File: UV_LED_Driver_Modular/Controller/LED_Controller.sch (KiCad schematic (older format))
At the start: 9 parts, among them J1 Barrel_Jack, J2 Conn_01x05, SW1 SW_SPST, U1 STM32L011D4Px, U2 LP3992-33B5F

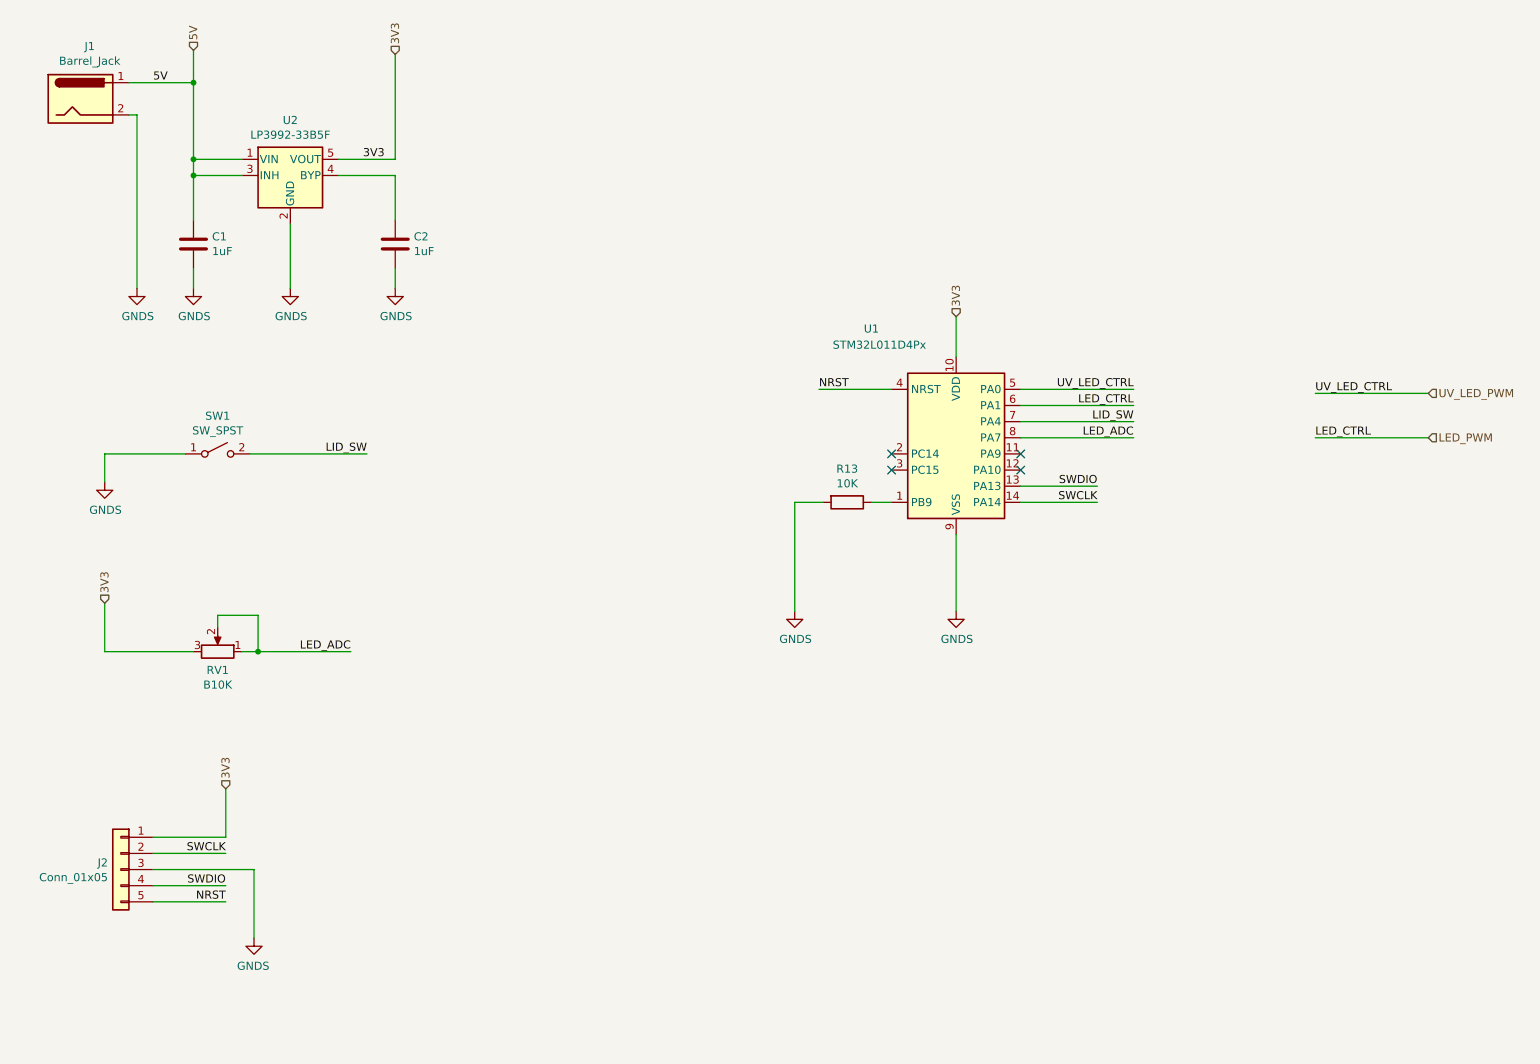
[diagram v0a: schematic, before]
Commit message: Changed TO225 NPN (MJE340) to SOT223 NPN (PZT2222A)
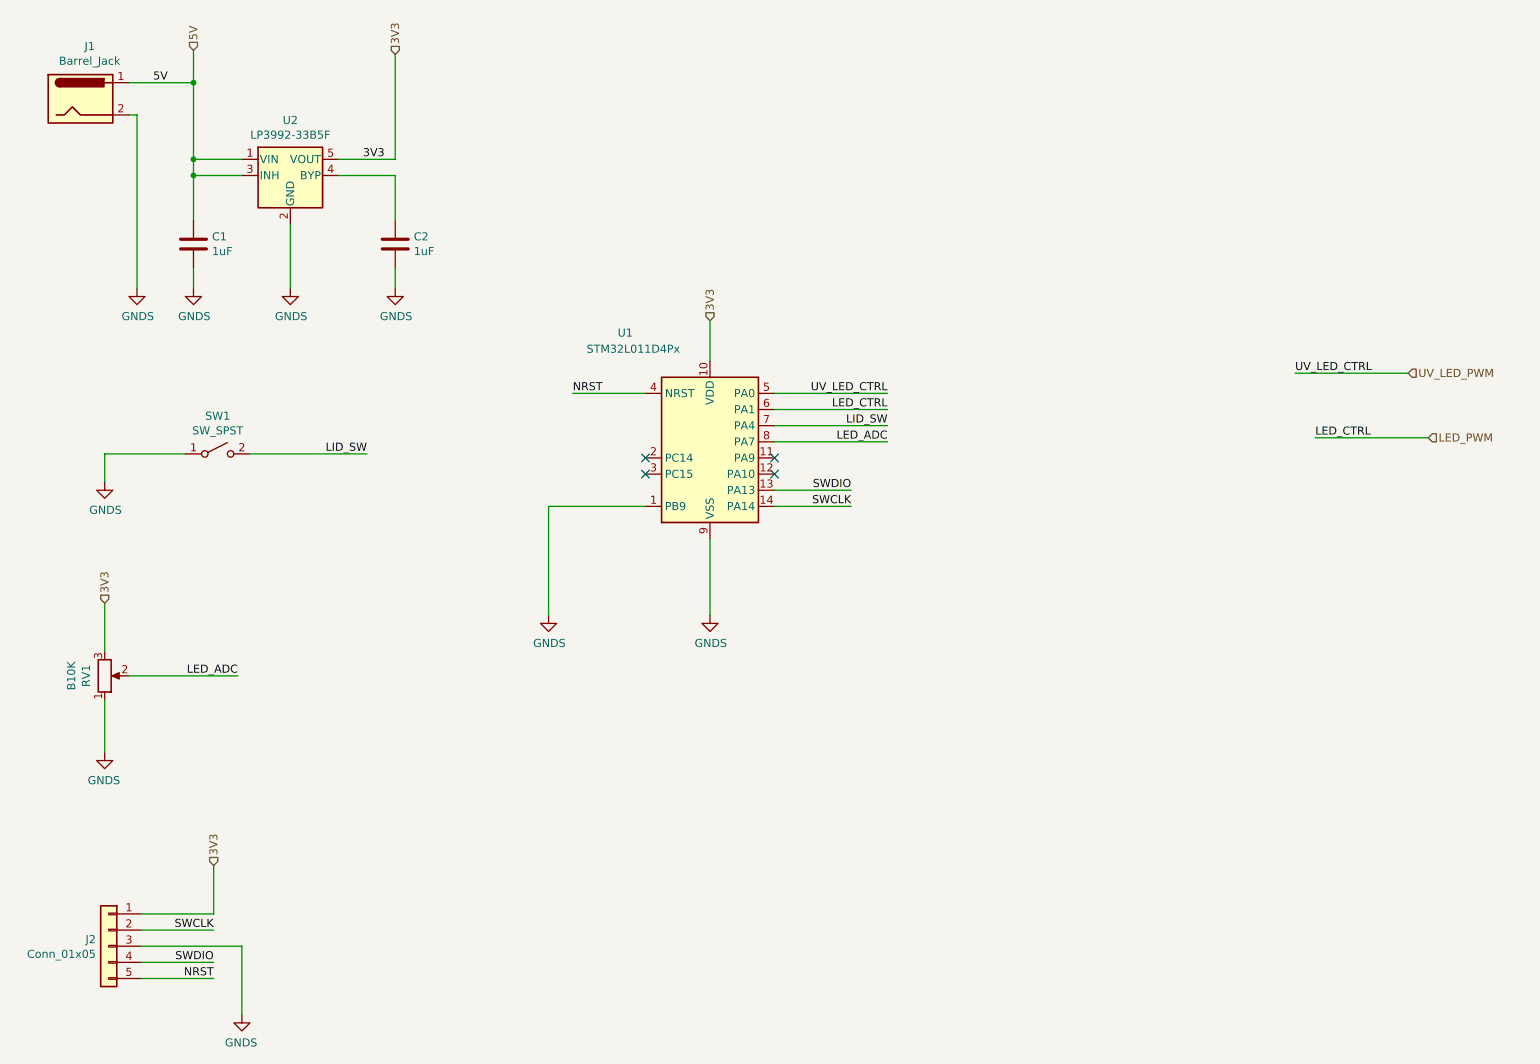
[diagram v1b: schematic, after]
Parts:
- removed R13: 10K, Resistor_SMD:R_1206_3216Metric_Pad1.42x1.75mm_HandSolder, symbol Device:R
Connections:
- net GNDS: now also RV1.1, U1.1 (PB9)
- net LED_ADC: no longer RV1.1
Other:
- moved on the sheet: J2, RV1, U1
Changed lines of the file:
@@
 $Descr A4 11693 8268
 encoding utf-8
-Sheet 6 2
+Sheet 2 2
 Title ""
 Date ""
@@
 $EndDescr
 Wire Wire Line
-	2075 6025 2525 6025
-Wire Wire Line
-	2075 6125 2525 6125
-Text Label 2525 6125 2    50   ~ 0
+	2000 6500 2450 6500
+Wire Wire Line
+	2000 6600 2450 6600
+Text Label 2450 6600 2    50   ~ 0
 SWCLK
-Text Label 2525 6325 2    50   ~ 0
+Text Label 2450 6800 2    50   ~ 0
 SWDIO
-Text Label 2525 6425 2    50   ~ 0
+Text Label 2450 6900 2    50   ~ 0
 NRST
 $Comp
 L Connector_Generic:Conn_01x05 J2
 U 1 1 5EA63B2F
-P 1875 6225
-F 0 "J2" H 1955 6267 50  0000 L CNN
-F 1 "Conn_01x05" H 1955 6176 50  0000 L CNN
-F 2 "Connector_Molex:Molex_KK-254_AE-6410-05A_1x05_P2.54mm_Vertical" H 1875 6225 50  0001 C CNN
-F 3 "~" H 1875 6225 50  0001 C CNN
-	1    1875 6225
+P 1800 6700
+F 0 "J2" H 1880 6742 50  0000 L CNN
+F 1 "Conn_01x05" H 1880 6651 50  0000 L CNN
+F 2 "Connector_Molex:Molex_KK-254_AE-6410-05A_1x05_P2.54mm_Vertical" H 1800 6700 50  0001 C CNN
+F 3 "~" H 1800 6700 50  0001 C CNN
+	1    1800 6700
 	-1   0    0    -1
 $EndComp
 Wire Wire Line
-	2525 6325 2075 6325
-Wire Wire Line
-	2075 6425 2525 6425
-Wire Wire Line
-	2075 6225 2700 6225
-Wire Wire Line
-	2700 6225 2700 6650
+	2450 6800 2000 6800
+Wire Wire Line
+	2000 6900 2450 6900
+Wire Wire Line
+	2000 6700 2625 6700
+Wire Wire Line
+	2625 6700 2625 7125
 $Comp
 L power:GNDS #PWR018
 U 1 1 5EA63B39
-P 2700 6650
-F 0 "#PWR018" H 2700 6400 50  0001 C CNN
-F 1 "GNDS" H 2705 6477 50  0000 C CNN
-F 2 "" H 2700 6650 50  0001 C CNN
-F 3 "" H 2700 6650 50  0001 C CNN
-	1    2700 6650
+P 2625 7125
+F 0 "#PWR018" H 2625 6875 50  0001 C CNN
+F 1 "GNDS" H 2630 6952 50  0000 C CNN
+F 2 "" H 2625 7125 50  0001 C CNN
+F 3 "" H 2625 7125 50  0001 C CNN
+	1    2625 7125
 	-1   0    0    -1
 $EndComp
-Text Label 6200 3250 0    50   ~ 0
+Text Label 4675 3275 0    50   ~ 0
 NRST
 Wire Wire Line
-	6650 3250 6200 3250
-Wire Wire Line
-	6650 3950 6525 3950
-Wire Wire Line
-	6050 3950 6050 4625
+	5125 3275 4675 3275
+Wire Wire Line
+	4525 3975 4525 4650
 $Comp
 L power:GNDS #PWR021
 U 1 1 5EA63B43
-P 6050 4625
-F 0 "#PWR021" H 6050 4375 50  0001 C CNN
-F 1 "GNDS" H 6055 4452 50  0000 C CNN
-F 2 "" H 6050 4625 50  0001 C CNN
-F 3 "" H 6050 4625 50  0001 C CNN
-	1    6050 4625
-	1    0    0    -1
-$EndComp
-NoConn ~ 6650 3750
-NoConn ~ 6650 3650
-NoConn ~ 7450 3750
-NoConn ~ 7450 3650
-Wire Wire Line
-	7450 3850 7925 3850
+P 4525 4650
+F 0 "#PWR021" H 4525 4400 50  0001 C CNN
+F 1 "GNDS" H 4530 4477 50  0000 C CNN
+F 2 "" H 4525 4650 50  0001 C CNN
+F 3 "" H 4525 4650 50  0001 C CNN
+	1    4525 4650
+	1    0    0    -1
+$EndComp
+NoConn ~ 5125 3775
+NoConn ~ 5125 3675
+NoConn ~ 5925 3775
+NoConn ~ 5925 3675
+Wire Wire Line
+	5925 3875 6400 3875
 $Comp
 L MCU_ST_STM32L0:STM32L011D4Px U1
 U 1 1 5EA63B4E
-P 7050 3550
-F 0 "U1" H 6525 4225 50  0000 C CNN
-F 1 "STM32L011D4Px" H 6575 4125 50  0000 C CNN
-F 2 "Package_SO:TSSOP-14_4.4x5mm_P0.65mm" H 6750 3050 50  0001 R CNN
-F 3 "http://www.st.com/st-web-ui/static/active/en/resource/technical/document/datasheet/DM00206508.pdf" H 7050 3550 50  0001 C CNN
-	1    7050 3550
-	1    0    0    -1
-$EndComp
-Wire Wire Line
-	7450 3950 7925 3950
-Text Label 7925 3950 2    50   ~ 0
+P 5525 3575
+F 0 "U1" H 5000 4250 50  0000 C CNN
+F 1 "STM32L011D4Px" H 5050 4150 50  0000 C CNN
+F 2 "Package_SO:TSSOP-14_4.4x5mm_P0.65mm" H 5225 3075 50  0001 R CNN
+F 3 "http://www.st.com/st-web-ui/static/active/en/resource/technical/document/datasheet/DM00206508.pdf" H 5525 3575 50  0001 C CNN
+	1    5525 3575
+	1    0    0    -1
+$EndComp
+Wire Wire Line
+	5925 3975 6400 3975
+Text Label 6400 3975 2    50   ~ 0
 SWCLK
-Text Label 7925 3850 2    50   ~ 0
+Text Label 6400 3875 2    50   ~ 0
 SWDIO
 Wire Wire Line
-	7050 3050 7050 2800
-Wire Wire Line
-	7050 4150 7050 4625
+	5525 3075 5525 2825
+Wire Wire Line
+	5525 4175 5525 4650
 $Comp
 L power:GNDS #PWR022
 U 1 1 5EA63B5F
-P 7050 4625
-F 0 "#PWR022" H 7050 4375 50  0001 C CNN
-F 1 "GNDS" H 7055 4452 50  0000 C CNN
-F 2 "" H 7050 4625 50  0001 C CNN
-F 3 "" H 7050 4625 50  0001 C CNN
-	1    7050 4625
+P 5525 4650
+F 0 "#PWR022" H 5525 4400 50  0001 C CNN
+F 1 "GNDS" H 5530 4477 50  0000 C CNN
+F 2 "" H 5525 4650 50  0001 C CNN
+F 3 "" H 5525 4650 50  0001 C CNN
+	1    5525 4650
 	1    0    0    -1
 $EndComp
@@
 LID_SW
 Wire Wire Line
-	7450 3450 8150 3450
-Text Label 8150 3450 2    50   ~ 0
+	5925 3475 6625 3475
+Text Label 6625 3475 2    50   ~ 0
 LID_SW
 $Comp
@@
 	2325 1350 2325 1150
 Connection ~ 2325 1350
-$Comp
-L Device:R R13
-U 1 1 5EA63BD8
-P 6375 3950
-F 0 "R13" V 6168 3950 50  0000 C CNN
-F 1 "10K" V 6259 3950 50  0000 C CNN
-F 2 "Resistor_SMD:R_1206_3216Metric_Pad1.42x1.75mm_HandSolder" V 6305 3950 50  0001 C CNN
-F 3 "~" H 6375 3950 50  0001 C CNN
-	1    6375 3950
-	0    1    1    0
-$EndComp
-Wire Wire Line
-	6225 3950 6050 3950
-Wire Wire Line
-	7450 3250 8150 3250
-Text Label 8150 3250 2    50   ~ 0
+Wire Wire Line
+	5925 3275 6625 3275
+Text Label 6625 3275 2    50   ~ 0
 UV_LED_CTRL
 Wire Wire Line
-	7450 3350 8150 3350
-Text Label 8150 3350 2    50   ~ 0
+	5925 3375 6625 3375
+Text Label 6625 3375 2    50   ~ 0
 LED_CTRL
 Wire Wire Line
-	7450 3550 8150 3550
-Text Label 8150 3550 2    50   ~ 0
+	5925 3575 6625 3575
+Text Label 6625 3575 2    50   ~ 0
 LED_ADC
 $Comp
 L Device:R_POT RV1
 U 1 1 5EA63BE5
-P 2475 4875
-F 0 "RV1" V 2360 4875 50  0000 C CNN
-F 1 "B10K" V 2269 4875 50  0000 C CNN
-F 2 "Connector_Molex:Molex_KK-254_AE-6410-03A_1x03_P2.54mm_Vertical" H 2475 4875 50  0001 C CNN
-F 3 "~" H 2475 4875 50  0001 C CNN
-	1    2475 4875
-	0    1    -1   0
-$EndComp
-Wire Wire Line
-	2625 4875 2725 4875
-Wire Wire Line
-	2325 4875 1775 4875
+P 1775 5025
+F 0 "RV1" V 1660 5025 50  0000 C CNN
+F 1 "B10K" V 1569 5025 50  0000 C CNN
+F 2 "Connector_Molex:Molex_KK-254_AE-6410-03A_1x03_P2.54mm_Vertical" H 1775 5025 50  0001 C CNN
+F 3 "~" H 1775 5025 50  0001 C CNN
+	1    1775 5025
+	1    0    0    1
+$EndComp
 Wire Wire Line
 	1775 4875 1775 4575
-Wire Wire Line
-	2475 4650 2725 4650
-Wire Wire Line
-	2725 4650 2725 4875
-Wire Wire Line
-	2475 4650 2475 4725
-Connection ~ 2725 4875
-Wire Wire Line
-	2725 4875 3300 4875
-Text Label 3300 4875 2    50   ~ 0
+Text Label 2600 5025 2    50   ~ 0
 LED_ADC
-Text HLabel 9975 3275 2    50   Input ~ 0
+Text HLabel 9850 3150 2    50   Input ~ 0
 UV_LED_PWM
 Text HLabel 9975 3550 2    50   Input ~ 0
 LED_PWM
 Wire Wire Line
-	9975 3275 9275 3275
-Text Label 9275 3275 0    50   ~ 0
+	9850 3150 9150 3150
+Text Label 9150 3150 0    50   ~ 0
 UV_LED_CTRL
 Wire Wire Line
@@
 Text Label 3375 1825 0    50   ~ 0
 3V3
-Text HLabel 7050 2800 1    50   Input ~ 0
+Text HLabel 5525 2825 1    50   Input ~ 0
 3V3
 Text HLabel 1775 4575 1    50   Input ~ 0
 3V3
 Wire Wire Line
-	2525 6025 2525 5725
-Text HLabel 2525 5725 1    50   Input ~ 0
+	2450 6500 2450 6200
+Text HLabel 2450 6200 1    50   Input ~ 0
 3V3
 Text Label 2075 1350 0    50   ~ 0
@@
 Wire Wire Line
 	1975 1550 1975 2625
+Wire Wire Line
+	1925 5025 2600 5025
+Wire Wire Line
+	1775 5175 1775 5500
+$Comp
+L power:GNDS #PWR0108
+U 1 1 5EB135AB
+P 1775 5500
+F 0 "#PWR0108" H 1775 5250 50  0001 C CNN
+F 1 "GNDS" H 1780 5327 50  0000 C CNN
+F 2 "" H 1775 5500 50  0001 C CNN
+F 3 "" H 1775 5500 50  0001 C CNN
+	1    1775 5500
+	-1   0    0    -1
+$EndComp
+Wire Wire Line
+	4525 3975 5125 3975
 $EndSCHEMATC

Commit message: updated
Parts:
- added JP1: Jumper_NC_Small, Jumper:SolderJumper-2_P1.3mm_Bridged_Pad1.0x1.5mm, symbol Device:Jumper_NC_Small
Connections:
- net GNDS: now also JP1.1; no longer U1.1 (PB9)
- net STATUS_PWM: now reaches U1.12 (PA10)
- new net: JP1.2, U1.1 (PB9)
- no-connect marks 4 -> 3
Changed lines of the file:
@@
 NoConn ~ 5125 3775
 NoConn ~ 5125 3675
-NoConn ~ 5925 3775
 NoConn ~ 5925 3675
 Wire Wire Line
@@
 F 1 "LP3992-33B5F" H 2925 2176 50  0000 C CNN
 F 2 "Package_TO_SOT_SMD:TSOT-23-5" H 2925 2250 50  0001 C CIN
-F 3 "${KIPRJMOD}/../datasheets/LOWPOWER-LP3992-33B5F_C324570.pdf" H 2925 1975 50  0001 C CNN
+F 3 "https://datasheet.lcsc.com/szlcsc/1811081106_LOWPOWER-LP3992-33B5F_C324570.pdf" H 2925 1975 50  0001 C CNN
 	1    2925 1925
 	1    0    0    -1
@@
 $EndComp
 Wire Wire Line
-	4525 3975 5125 3975
+	4525 3975 4675 3975
+Wire Wire Line
+	4875 3975 5125 3975
+$Comp
+L Device:Jumper_NC_Small JP1
+U 1 1 5EA6AD24
+P 4775 3975
+F 0 "JP1" H 4775 4096 50  0000 C CNN
+F 1 "Jumper_NC_Small" H 4775 4096 50  0001 C CNN
+F 2 "Jumper:SolderJumper-2_P1.3mm_Bridged_Pad1.0x1.5mm" H 4775 3975 50  0001 C CNN
+F 3 "~" H 4775 3975 50  0001 C CNN
+	1    4775 3975
+	1    0    0    -1
+$EndComp
+Wire Wire Line
+	5925 3775 6625 3775
+Text Label 6625 3775 2    50   ~ 0
+STATUS_CTRL
+Wire Wire Line
+	9875 3900 9175 3900
+Text Label 9175 3900 0    50   ~ 0
+STATUS_CTRL
+Text HLabel 9875 3900 2    50   Input ~ 0
+STATUS_PWM
 $EndSCHEMATC

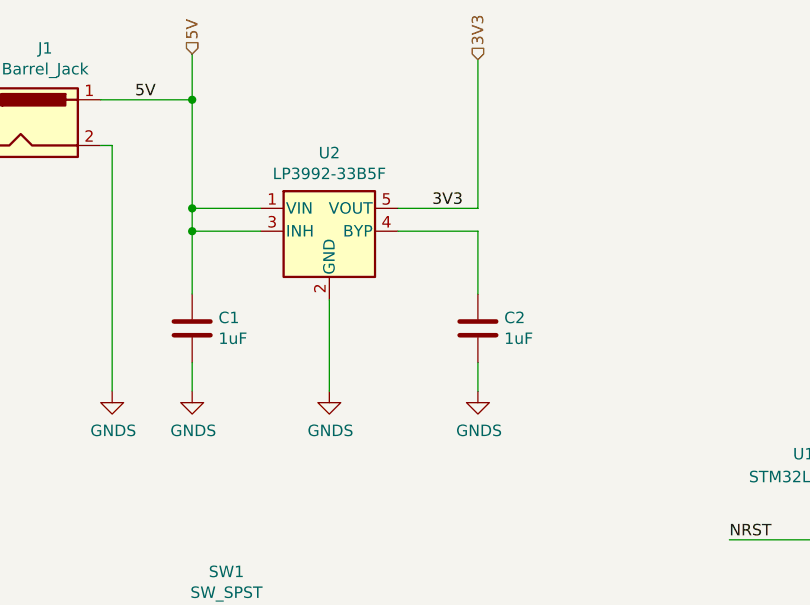
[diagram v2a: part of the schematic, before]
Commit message: changed controller module LDO from SOT23 to SOT223
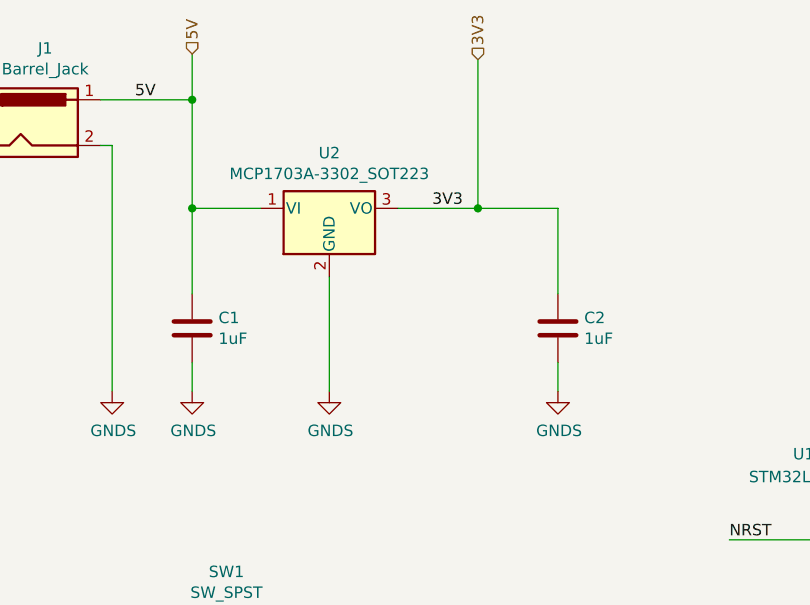
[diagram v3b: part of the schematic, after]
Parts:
- removed U2: LP3992-33B5F, Package_TO_SOT_SMD:TSOT-23-5, symbol Regulator_Linear:LD3985G33R_TSOT23
- added U2: MCP1703A-3302_SOT223, Package_TO_SOT_SMD:SOT-223-3_TabPin2, symbol Regulator_Linear:MCP1703A-3302_SOT223
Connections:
- net 3V3: now also C2.1, U2.3 (VO)
- net 5V: now also U2.1 (VI)
- net GNDS: now also U2.2 (GND)
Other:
- moved on the sheet: C2
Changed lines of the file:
@@
 Text Label 6625 3475 2    50   ~ 0
 LID_SW
-$Comp
-L Regulator_Linear:LD3985G33R_TSOT23 U2
-U 1 1 5EA63B77
-P 2925 1925
-F 0 "U2" H 2925 2267 50  0000 C CNN
-F 1 "LP3992-33B5F" H 2925 2176 50  0000 C CNN
-F 2 "Package_TO_SOT_SMD:TSOT-23-5" H 2925 2250 50  0001 C CIN
-F 3 "https://datasheet.lcsc.com/szlcsc/1811081106_LOWPOWER-LP3992-33B5F_C324570.pdf" H 2925 1975 50  0001 C CNN
-	1    2925 1925
-	1    0    0    -1
-$EndComp
 Wire Wire Line
 	2625 1825 2325 1825
-Wire Wire Line
-	2625 1925 2325 1925
-Wire Wire Line
-	2325 1925 2325 1825
 Connection ~ 2325 1825
 Wire Wire Line
-	2325 1925 2325 2200
-Connection ~ 2325 1925
-Wire Wire Line
 	3225 1825 3575 1825
 Wire Wire Line
 	3575 1825 3575 1175
 Wire Wire Line
-	3225 1925 3575 1925
-Wire Wire Line
-	3575 1925 3575 2200
+	3575 1825 3925 1825
+Wire Wire Line
+	3925 1825 3925 2200
 $Comp
 L Device:C C2
 U 1 1 5EA63B87
-P 3575 2350
-F 0 "C2" H 3690 2396 50  0000 L CNN
-F 1 "1uF" H 3690 2305 50  0000 L CNN
-F 2 "Capacitor_SMD:C_1206_3216Metric_Pad1.42x1.75mm_HandSolder" H 3613 2200 50  0001 C CNN
-F 3 "~" H 3575 2350 50  0001 C CNN
-	1    3575 2350
+P 3925 2350
+F 0 "C2" H 4040 2396 50  0000 L CNN
+F 1 "1uF" H 4040 2305 50  0000 L CNN
+F 2 "Capacitor_SMD:C_1206_3216Metric_Pad1.42x1.75mm_HandSolder" H 3963 2200 50  0001 C CNN
+F 3 "~" H 3925 2350 50  0001 C CNN
+	1    3925 2350
 	1    0    0    -1
 $EndComp
@@
 $EndComp
 Wire Wire Line
-	3575 2500 3575 2625
+	3925 2500 3925 2625
 $Comp
 L power:GNDS #PWR020
 U 1 1 5EA63B9B
-P 3575 2625
-F 0 "#PWR020" H 3575 2375 50  0001 C CNN
-F 1 "GNDS" H 3580 2452 50  0000 C CNN
-F 2 "" H 3575 2625 50  0001 C CNN
-F 3 "" H 3575 2625 50  0001 C CNN
-	1    3575 2625
-	1    0    0    -1
-$EndComp
-Wire Wire Line
-	2925 2225 2925 2625
+P 3925 2625
+F 0 "#PWR020" H 3925 2375 50  0001 C CNN
+F 1 "GNDS" H 3930 2452 50  0000 C CNN
+F 2 "" H 3925 2625 50  0001 C CNN
+F 3 "" H 3925 2625 50  0001 C CNN
+	1    3925 2625
+	1    0    0    -1
+$EndComp
+Wire Wire Line
+	2925 2125 2925 2625
 $Comp
 L power:GNDS #PWR019
@@
 Text HLabel 9875 3900 2    50   Input ~ 0
 STATUS_PWM
+$Comp
+L Regulator_Linear:MCP1703A-3302_SOT223 U2
+U 1 1 5EAEE911
+P 2925 1825
+F 0 "U2" H 2925 2067 50  0000 C CNN
+F 1 "MCP1703A-3302_SOT223" H 2925 1976 50  0000 C CNN
+F 2 "Package_TO_SOT_SMD:SOT-223-3_TabPin2" H 2925 2025 50  0001 C CNN
+F 3 "http://ww1.microchip.com/downloads/en/DeviceDoc/20005122B.pdf" H 2925 1775 50  0001 C CNN
+	1    2925 1825
+	1    0    0    -1
+$EndComp
+Wire Wire Line
+	2325 1825 2325 2200
+Connection ~ 3575 1825
 $EndSCHEMATC
